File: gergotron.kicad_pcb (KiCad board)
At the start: 2 copper layers, 68.6 x 53.3 mm, 14 parts, among them J1 KMDGX-6S-BS, J2 KMDGX-6S-BS, P1 Power, P2 Analog, P3 Digital, P4 Digital, P5 CONN_01X01, P6 CONN_01X01, P7 CONN_01X01, P8 CONN_01X01, U1 TXB0104D

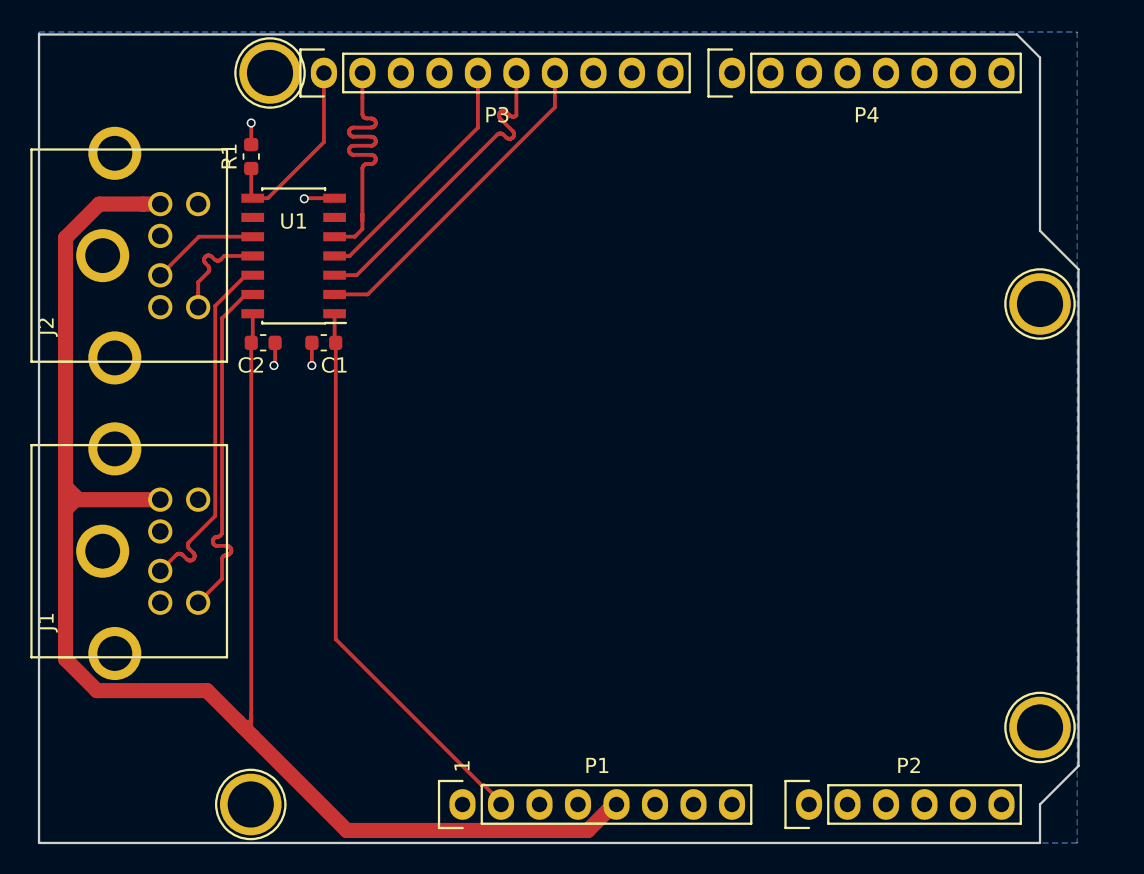
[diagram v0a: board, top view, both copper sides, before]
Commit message: Add audio in
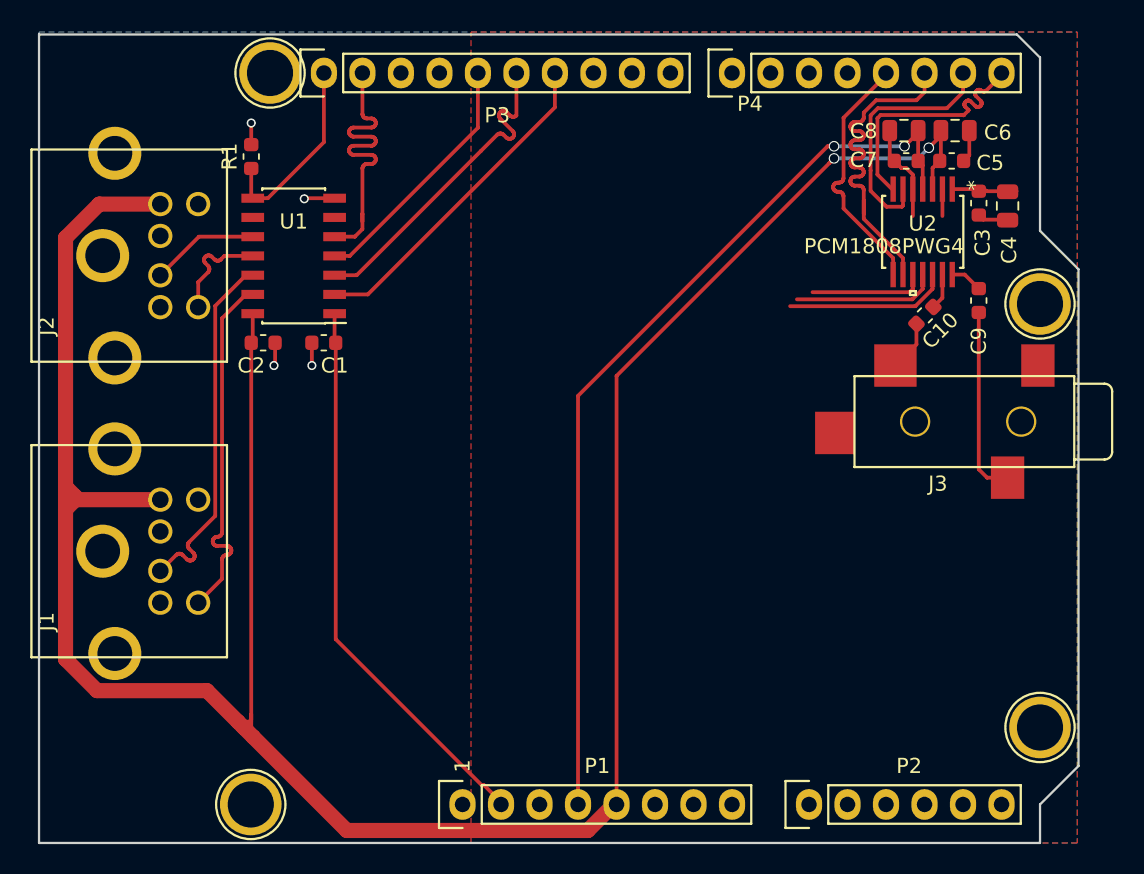
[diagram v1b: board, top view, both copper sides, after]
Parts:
- added C10: 1μF, Capacitor_SMD:C_0603_1608Metric, F.Cu at (169.4, 91.6)
- added C3: 0.1μF, Capacitor_SMD:C_0603_1608Metric, F.Cu at (173.0, 84.2)
- added C4: 10μF, Capacitor_SMD:C_0805_2012Metric, F.Cu at (174.9, 84.3)
- added C5: 0.1μF, Capacitor_SMD:C_0603_1608Metric, F.Cu at (171.2, 81.4)
- added C6: 10μF, Capacitor_SMD:C_0805_2012Metric, F.Cu at (171.4, 79.4)
- added C7: 0.1μF, Capacitor_SMD:C_0603_1608Metric, F.Cu at (168.2, 81.4)
- added C8: 10μF, Capacitor_SMD:C_0805_2012Metric, F.Cu at (168.1, 79.4)
- added C9: 1μF, Capacitor_SMD:C_0603_1608Metric, F.Cu at (173.0, 90.6)
- added J3: AudioJack3_TRS_TN, gergotron:sj-352x-smt, F.Cu at (179.3, 98.6)
- added U2: PCM1808PWG4, pcm1808:PCM1808PWG4, F.Cu at (169.3, 86.0)
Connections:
- P4 pad 5: Net-(P4-Pad5) -> BCK
- P4 pad 6: Net-(P4-Pad6) -> DOUT
- P4 pad 7: Net-(P4-Pad7) -> SCKI
- P4 pad 8: Net-(P4-Pad8) -> LRCK
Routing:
- net +5V: track 115.1 -> 176.1 mm, vias 0 -> 2
- net +3V3: track 0.00 -> 60.7 mm, vias 0 -> 2
- net DOUT: track 0.00 -> 23.5 mm
- net SCKI: track 0.00 -> 16.8 mm
- net LRCK: track 0.00 -> 16.7 mm
- net BCK: track 0.00 -> 16.7 mm
- net GND: track 6.47 -> 19.0 mm
- net RIN: track 0.00 -> 12.5 mm
- net Net-(U2-Pad12): track 0.00 -> 10.8 mm
- net Net-(U2-Pad11): track 0.00 -> 9.53 mm
- net Net-(U2-Pad10): track 0.00 -> 7.66 mm
- net Net-(C3-Pad1): track 0.00 -> 4.01 mm
- net LIN: track 0.00 -> 3.33 mm
- net Net-(C10-Pad1): track 0.00 -> 2.38 mm
- net Net-(C9-Pad1): track 0.00 -> 2.13 mm
- added copper zone on F.Cu, net GND

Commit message: Add oled display
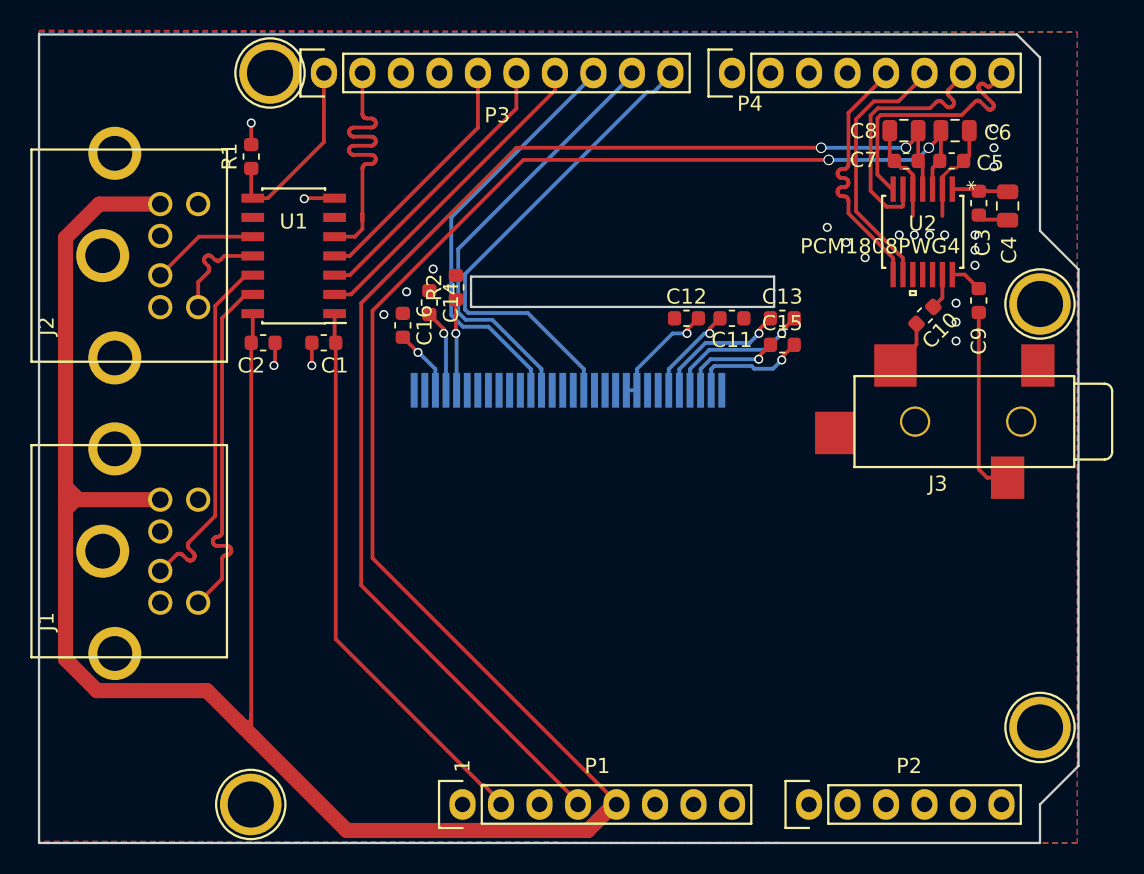
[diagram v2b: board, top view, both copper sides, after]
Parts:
- added C11: 1μF, Capacitor_SMD:C_0603_1608Metric, F.Cu at (156.7, 91.8)
- added C12: 1μF, Capacitor_SMD:C_0603_1608Metric, F.Cu at (153.7, 91.8)
- added C13: 1μF, Capacitor_SMD:C_0603_1608Metric, F.Cu at (160.0, 91.8)
- added C14: 2.2μF, Capacitor_SMD:C_0603_1608Metric, F.Cu at (136.8, 90.7)
- added C15: 1μF, Capacitor_SMD:C_0603_1608Metric, F.Cu at (160.0, 93.5)
- added C16: 2.2μF, Capacitor_SMD:C_0603_1608Metric, F.Cu at (135.0, 92.2)
- added CON1: ER-OLED-FPC30, gergotron:er-oled-fpc30-flipped, B.Cu at (145.9, 97.8)
- added R2: 400kΩ, Resistor_SMD:R_0603_1608Metric, F.Cu at (138.5, 89.7)
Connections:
- P3 pad 10: Net-(P3-Pad10) -> oled_res
- P3 pad 8: Net-(P3-Pad8) -> oled_sdin
- P3 pad 9: Net-(P3-Pad9) -> oled_sclk
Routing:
- net oled_res: track 0.00 -> 32.3 mm
- net oled_sclk: track 0.00 -> 29.0 mm
- net oled_sdin: track 0.00 -> 28.0 mm
- net +5V: track 176.1 -> 201.4 mm
- net +3V3: track 60.7 -> 84.7 mm
- net Net-(U2-Pad12): track 10.8 -> 0.00 mm
- net Net-(C13-Pad2): track 0.00 -> 9.77 mm, vias 0 -> 1
- net Net-(U2-Pad11): track 9.53 -> 0.00 mm
- net Net-(C13-Pad1): track 0.00 -> 8.94 mm, vias 0 -> 1
- net Net-(C15-Pad2): track 0.00 -> 7.79 mm, vias 0 -> 1
- net Net-(C12-Pad2): track 0.00 -> 7.69 mm, vias 0 -> 1
- net Net-(U2-Pad10): track 7.66 -> 0.00 mm
- net Net-(C15-Pad1): track 0.00 -> 6.77 mm, vias 0 -> 1
- net Net-(C11-Pad2): track 0.00 -> 6.36 mm, vias 0 -> 1
- net DOUT: track 23.5 -> 17.4 mm
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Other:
- outline, holes or cut-outs redrawn

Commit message: power to the oled
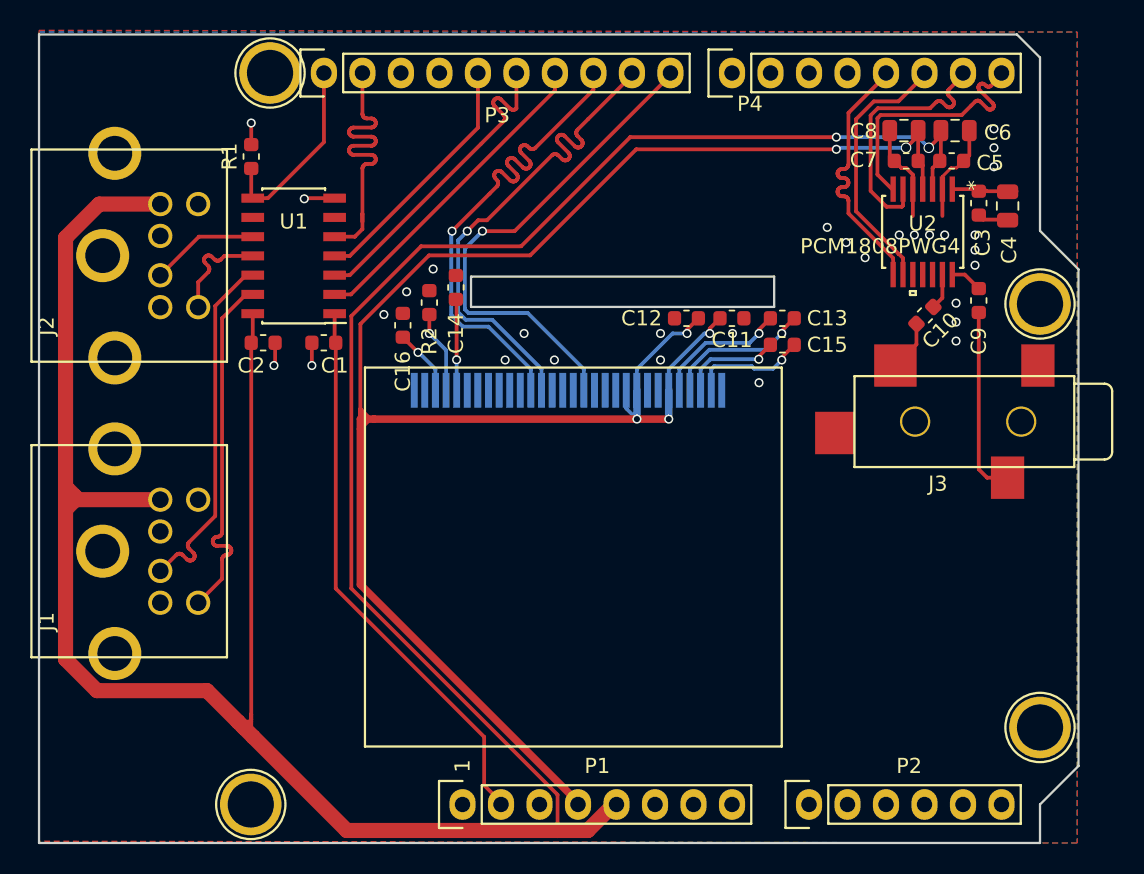
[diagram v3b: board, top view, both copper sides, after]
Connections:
- C11 pad 2: Net-(C11-Pad2) -> +3V3
- C12 pad 2: Net-(C12-Pad2) -> +3V3
- CON1 pad 10: Net-(C12-Pad2) -> +3V3
- CON1 pad 6: Net-(C11-Pad2) -> +3V3
- CON1 pad 9: Net-(C12-Pad2) -> +3V3
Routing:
- net +3V3: track 84.7 -> 128.1 mm, vias 2 -> 6
- net Net-(C12-Pad2): track 7.69 -> 0.00 mm, vias 1 -> 0
- net Net-(C11-Pad2): track 6.36 -> 0.00 mm, vias 1 -> 0
- net oled_sdin: track 28.0 -> 33.5 mm, vias 0 -> 1
- net oled_sclk: track 29.0 -> 33.5 mm, vias 0 -> 1
- net +5V: track 201.4 -> 204.0 mm
- net /MD: track 18.9 -> 21.3 mm
- net oled_res: track 32.3 -> 33.5 mm, vias 0 -> 1
- net GND: vias 23 -> 30

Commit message: Fiddle traces
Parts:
- added REF**: sj-352x-smt, gergotron:sj-352x-smt, F.Cu at (179.3, 111.0)
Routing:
- net SCKI: track 17.4 -> 57.9 mm
- net Net-(P4-Pad1): track 0.00 -> 33.6 mm
- net Net-(P4-Pad4): track 0.00 -> 32.9 mm
- net Net-(P4-Pad2): track 0.00 -> 32.1 mm
- net Net-(P4-Pad3): track 0.00 -> 31.4 mm

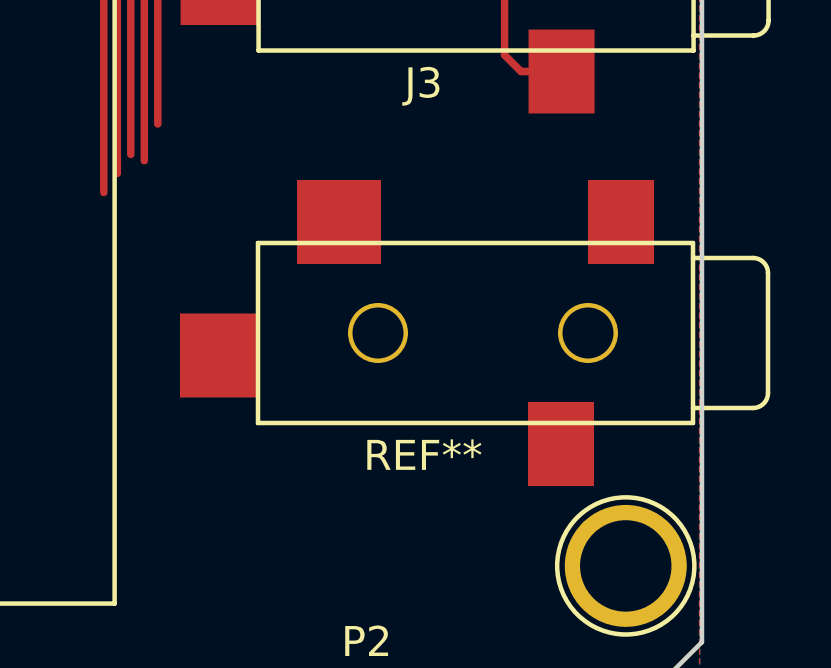
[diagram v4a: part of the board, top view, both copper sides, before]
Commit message: Tidy up schematic and connect unused data wires to gnd
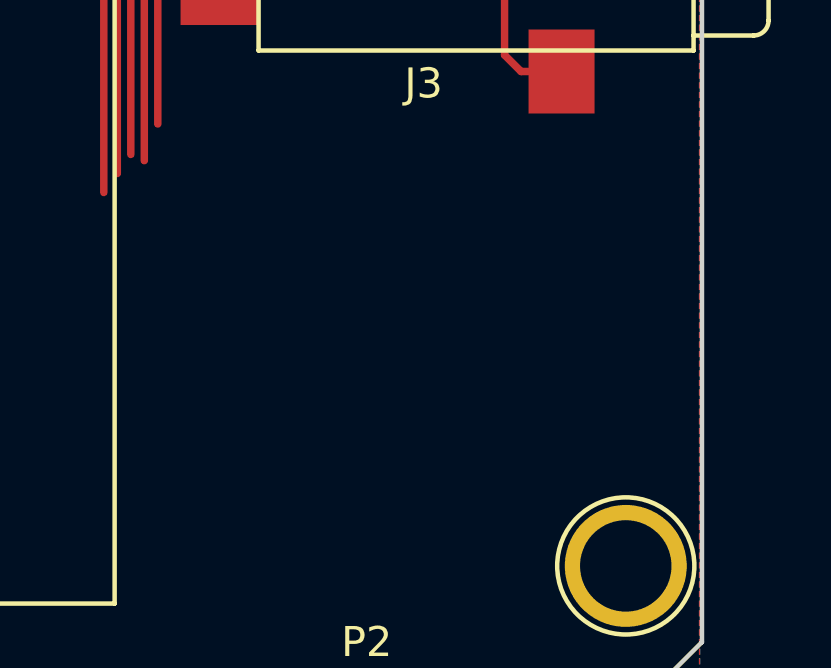
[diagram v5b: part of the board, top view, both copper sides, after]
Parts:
- removed REF**: sj-352x-smt, gergotron:sj-352x-smt
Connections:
- CON1 pad 22: Net-(CON1-Pad22) -> GND
- CON1 pad 23: Net-(CON1-Pad23) -> GND
- CON1 pad 24: Net-(CON1-Pad24) -> GND
- CON1 pad 25: Net-(CON1-Pad25) -> GND

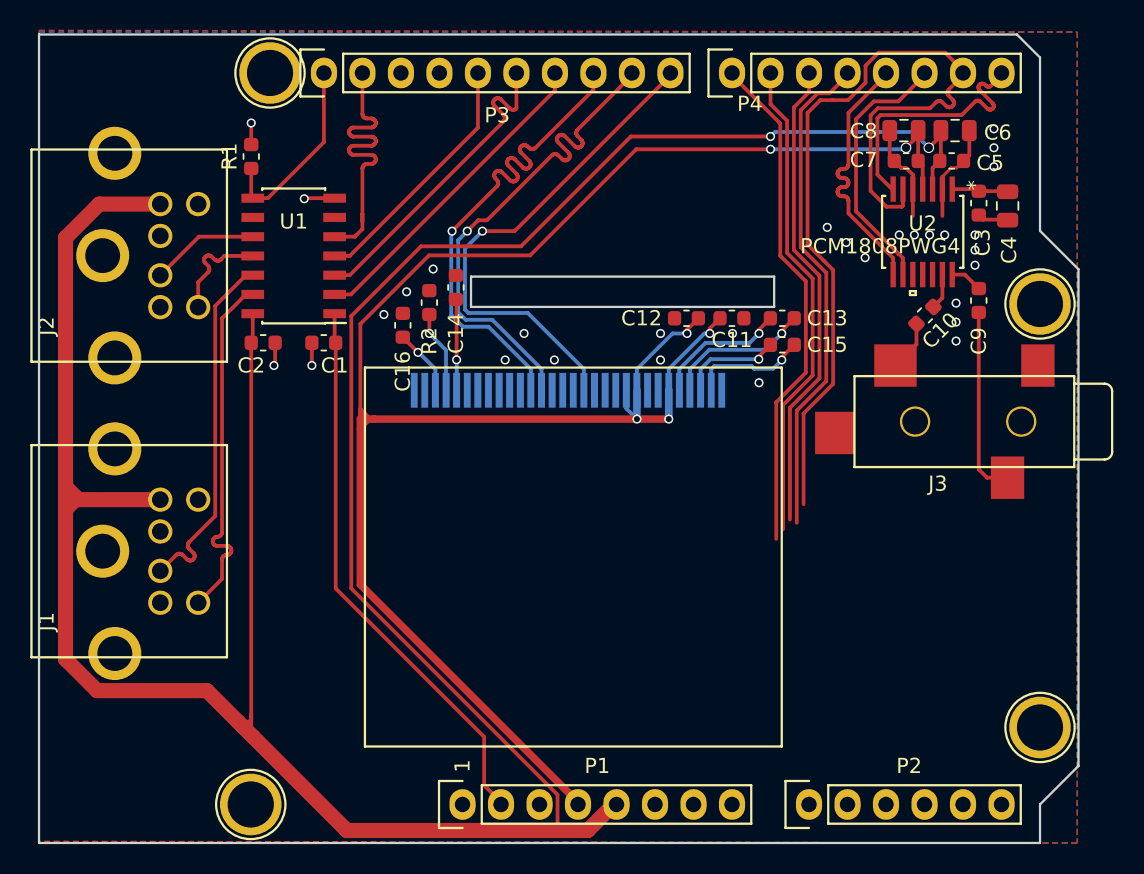
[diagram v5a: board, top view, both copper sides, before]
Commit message: Start work on the DAC
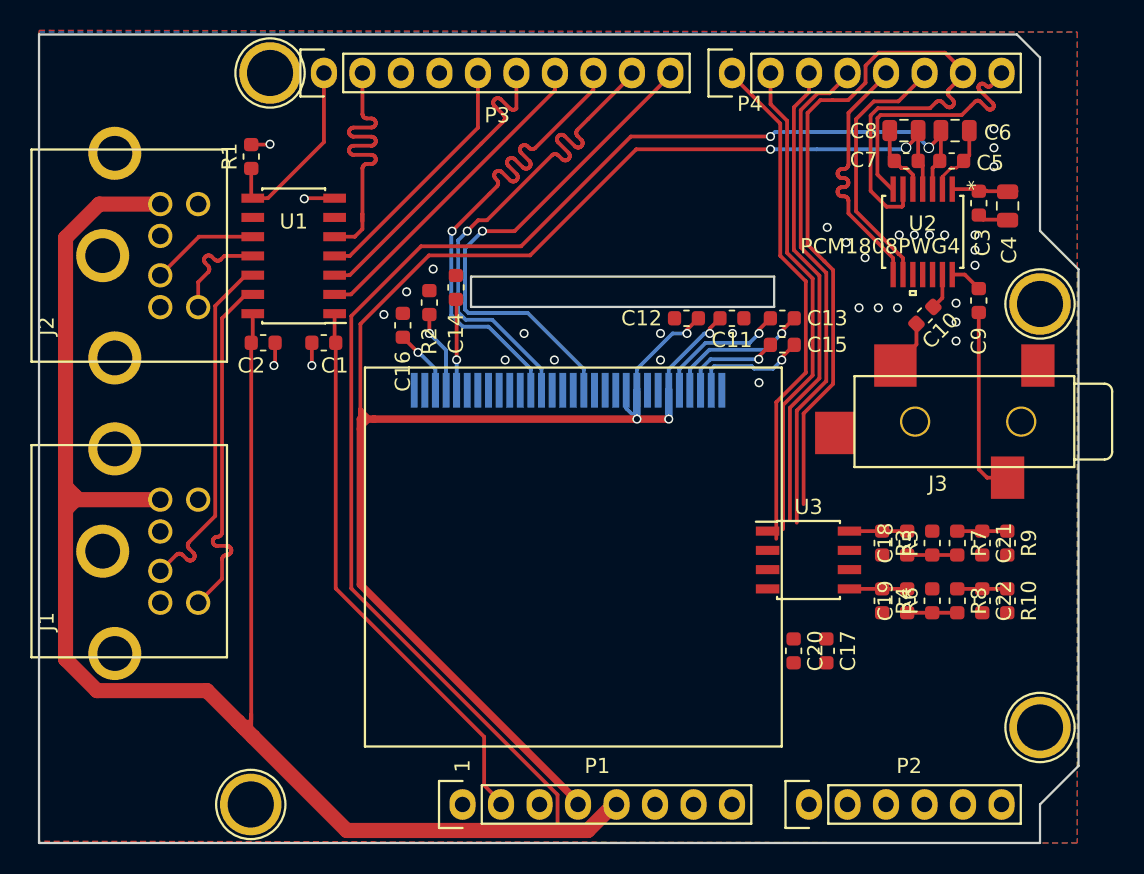
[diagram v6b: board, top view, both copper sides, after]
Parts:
- added C17: 0.1μF, Capacitor_SMD:C_0603_1608Metric, F.Cu at (162.9, 113.7)
- added C18: 3.3μF, Capacitor_SMD:C_0603_1608Metric, F.Cu at (168.3, 106.6)
- added C19: 3.3μF, Capacitor_SMD:C_0603_1608Metric, F.Cu at (168.3, 110.4)
- added C20: 1μF, Capacitor_SMD:C_0603_1608Metric, F.Cu at (160.8, 113.7)
- added C21: C, Capacitor_SMD:C_0603_1608Metric, F.Cu at (173.2, 106.6)
- added C22: C, Capacitor_SMD:C_0603_1608Metric, F.Cu at (173.2, 110.4)
- added R10: R_Small, Resistor_SMD:R_0603_1608Metric, F.Cu at (174.9, 110.4)
- added R3: 267kΩ, Resistor_SMD:R_0603_1608Metric, F.Cu at (166.6, 106.6)
- added R4: 267kΩ, Resistor_SMD:R_0603_1608Metric, F.Cu at (166.6, 110.4)
- added R5: 10kΩ, Resistor_SMD:R_0603_1608Metric, F.Cu at (169.9, 106.6)
- added R6: 10kΩ, Resistor_SMD:R_0603_1608Metric, F.Cu at (169.9, 110.4)
- added R7: 560Ω, Resistor_SMD:R_0603_1608Metric, F.Cu at (171.6, 106.6)
- added R8: 560Ω, Resistor_SMD:R_0603_1608Metric, F.Cu at (171.6, 110.4)
- added R9: R_Small, Resistor_SMD:R_0603_1608Metric, F.Cu at (174.9, 106.6)
- added U3: CS4334, Package_SO:SOIC-8_3.9x4.9mm_P1.27mm, F.Cu at (161.8, 107.7)
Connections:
- P4 pad 4: Net-(P4-Pad4) -> DOUT
- P4 pad 6: DOUT -> DIN
- U2 pad 10: Net-(U2-Pad10) -> GND
- U2 pad 11: Net-(U2-Pad11) -> GND
- U2 pad 12: Net-(U2-Pad12) -> GND
- U2 pad 9: DOUT -> DIN
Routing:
- net Net-(P4-Pad4): track 32.9 -> 0.00 mm
- net DIN: track 0.00 -> 17.4 mm
- net DOUT: track 17.4 -> 32.9 mm
- net Net-(C19-Pad2): track 0.00 -> 3.81 mm
- net Net-(C18-Pad2): track 0.00 -> 3.81 mm
- net GND: track 21.6 -> 17.9 mm, vias 30 -> 33
- net Net-(C22-Pad1): track 0.00 -> 3.30 mm
- net Net-(C21-Pad1): track 0.00 -> 3.30 mm
- net Net-(C19-Pad1): track 0.00 -> 3.30 mm
- net Net-(C18-Pad1): track 0.00 -> 3.30 mm
